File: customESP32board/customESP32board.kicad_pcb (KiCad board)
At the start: 2 copper layers, 55 x 55 mm, 43 parts, among them J1 USB_B_Micro, J2 Conn_01x16_Pin, J3 Conn_01x16_Pin, Q1 S8050, Q2 S8050, Q3 BSS138, Q4 BSS138, Q5 BSS138, SW1 SW_Push, SW2 SW_Push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

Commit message: updated routing
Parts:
- moved C6 0.10 mm to (139.5, 115.1)
- renumbered SW2 to BOOT, SW1 to RESET
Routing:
- net +3V3: track 104.7 -> 103.6 mm

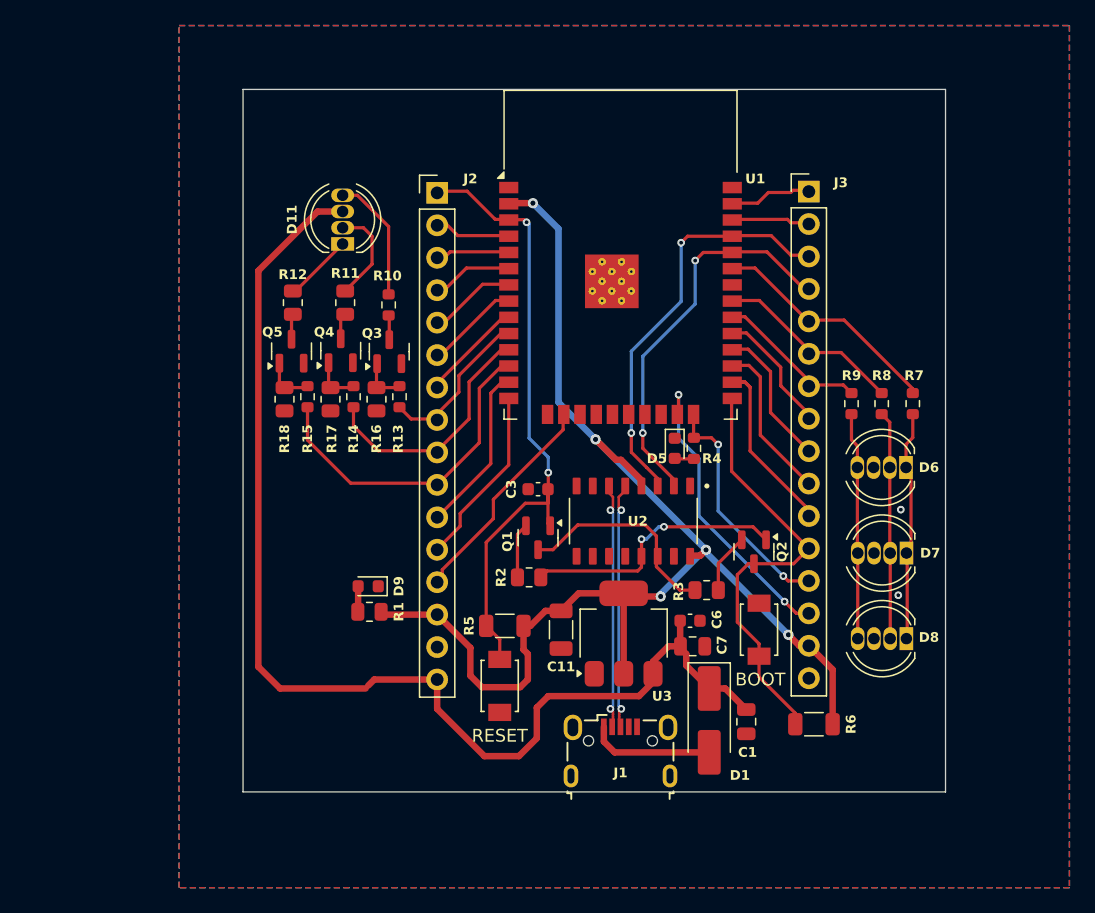
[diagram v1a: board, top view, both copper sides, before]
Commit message: adjusted placement to 0.1 mm grid
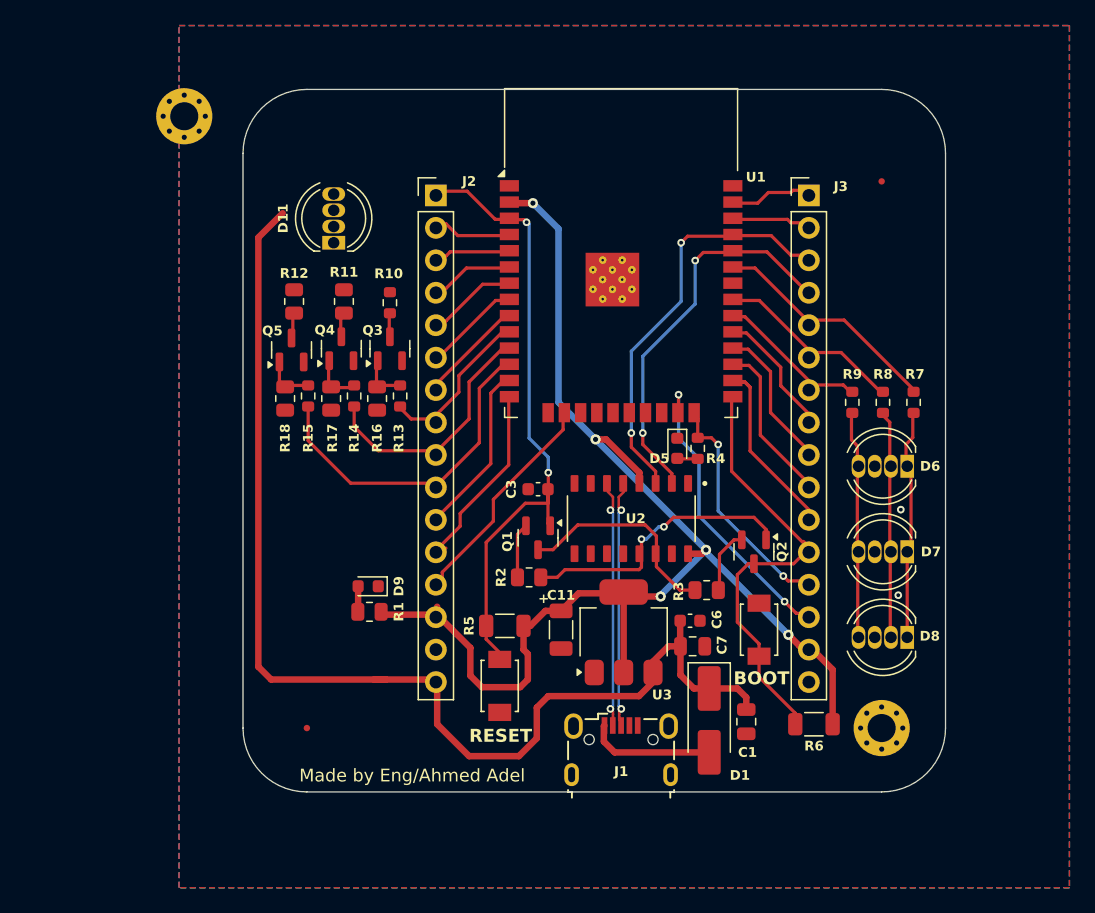
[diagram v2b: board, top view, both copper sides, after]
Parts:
- added FID1: Fiducial, Fiducial:Fiducial_0.5mm_Mask1.5mm, F.Cu at (109.5, 123.5)
- added FID2: Fiducial, Fiducial:Fiducial_0.5mm_Mask1.5mm, F.Cu at (154.5, 80.7)
- added H1: MountingHole_Pad, MountingHole:MountingHole_2.2mm_M2_Pad_Via, F.Cu at (99.9, 75.6)
- added H2: MountingHole_Pad, MountingHole:MountingHole_2.2mm_M2_Pad_Via, F.Cu at (154.5, 123.5)
- U2: value CH340C -> SOIC127P600X180-16N
- moved D11 0.71 mm to (111.6, 85.5)
- moved J3 0.30 mm to (148.8, 81.8)
- moved R4 0.30 mm to (140.1, 101.6)
- moved U2 0.26 mm to (134.9, 107.1)
- moved Q3 0.24 mm to (116.0, 93.8)
- moved J2 0.22 mm to (119.6, 81.8)
- moved D5 0.20 mm to (138.5, 101.6)
- moved R10 0.20 mm to (116.0, 90.2)
- moved Q4 0.17 mm to (112.2, 93.8)
- moved U1 0.14 mm to (134.1, 89.3)
- moved R8 0.14 mm to (154.6, 98.0)
- moved R11 0.14 mm to (112.4, 90.1)
- moved R12 0.14 mm to (108.5, 90.1)
- moved D6 0.14 mm to (156.5, 103.0)
- moved D8 0.12 mm to (156.5, 116.4)
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- renumbered RESET to SW1, BOOT to SW2
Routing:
- net Net-(D11-RK): track 9.92 -> 0.00 mm
- net Net-(D11-GK): track 7.73 -> 0.00 mm
- net Net-(D11-BK): track 5.43 -> 0.00 mm
- net DTR: track 21.0 -> 22.1 mm
- net +5V: track 92.8 -> 92.3 mm
- net ESP_IO14: track 13.9 -> 13.4 mm
- net ESP_IO27: track 26.8 -> 26.3 mm
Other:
- outline, holes or cut-outs redrawn
- board text added: "+"
- board text added: "BOOT"
- board text added: "Made by Eng/Ahmed Adel"
- board text added: "RESET"

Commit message: finalized board routing, generated gerbers and drill files also generated step file
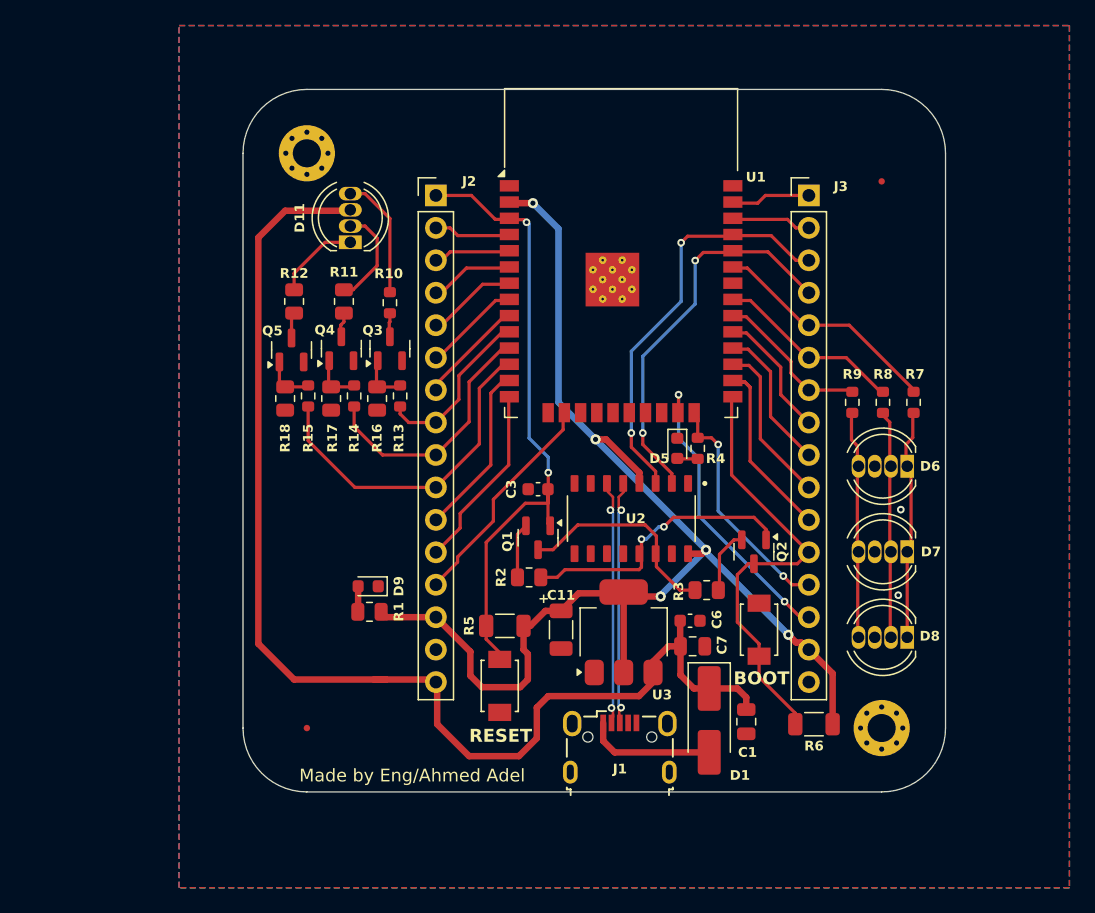
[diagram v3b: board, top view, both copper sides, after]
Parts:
- moved H1 10.0 mm to (109.5, 78.5)
- moved D11 1.30 mm to (112.9, 85.5)
- moved J1 0.22 mm to (134.0, 125.0)
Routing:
- net Net-(D11-RK): track 0.00 -> 9.68 mm
- net Net-(D11-GK): track 0.00 -> 8.03 mm
- net Net-(D11-BK): track 0.00 -> 6.69 mm
- net +5V: track 92.3 -> 96.6 mm
- net +3V3: track 103.7 -> 102.6 mm
- net ESP_IO0: track 35.1 -> 34.5 mm
